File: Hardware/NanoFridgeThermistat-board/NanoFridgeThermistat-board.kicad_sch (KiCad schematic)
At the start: 18 parts, among them J1 Connector_Thermistor, J2 Main_Connector, J3 CompressorMotor_Connector, J4 I2C_Conn, U1 MOC3042M

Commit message: Improved routing for hardware
Signed-off-by: bebenlebricolo <benoittarrade@hotmail.fr>
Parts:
- D2: footprint (none) -> LED_THT:LED_D3.0mm
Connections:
- net Trigger: now reaches D1.3 (G), R3.2, U1.4
- net SnubberResLow: now reaches C1.1, R5.1, R6.1, R7.1, R8.1
- net NeutralTriac: now reaches C1.2, D1.1 (A1), J3.2 (Pin_2), R3.1
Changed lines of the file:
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@@
   (junction (at 186.69 60.96) (diameter 0) (color 0 0 0 0)
+  )
+  (junction (at 186.69 69.85) (diameter 0) (color 0 0 0 0)
   )
   (junction (at 186.69 57.15) (diameter 0) (color 0 0 0 0)
@@
     (stroke (width 0) (type default))
   )
+  (wire (pts (xy 181.61 69.85) (xy 186.69 69.85))
+    (stroke (width 0) (type default))
+  )
   (wire (pts (xy 151.13 57.15) (xy 162.56 57.15))
     (stroke (width 0) (type default))
@@
     (effects (font (size 1.27 1.27)) (justify left bottom))
   )
+  (label "Trigger" (at 146.05 62.23 0) (fields_autoplaced)
+    (effects (font (size 1 1)) (justify left bottom))
+  )
+  (label "SnubberResLow" (at 181.61 69.85 180) (fields_autoplaced)
+    (effects (font (size 1.27 1.27)) (justify right bottom))
+  )
+  (label "NeutralTriac" (at 162.56 74.93 0) (fields_autoplaced)
+    (effects (font (size 1 1)) (justify left bottom))
+  )
+  (label "LiveTriac" (at 154.94 57.15 0) (fields_autoplaced)
+    (effects (font (size 1 1)) (justify left bottom))
+  )
   (global_label "SDA" (shape input) (at 172.72 133.35 0) (fields_autoplaced)
     (effects (font (size 1.27 1.27)) (justify left))
@@
     (property "Intersheetrefs" "${INTERSHEET_REFS}" (at 186.9537 123.19 0)
       (effects (font (size 1.27 1.27)) (justify left) hide)
+    )
+  )
+  (netclass_flag "" (length 2.54) (shape round) (at 196.85 68.58 180)
+    (effects (font (size 1.27 1.27)) (justify right bottom))
+    (property "Netclass" "SnubberResLow" (at 195.58 72.39 0)
+      (effects (font (size 1 1) italic) (justify left))
     )
   )
@@
       (effects (font (size 1.27 1.27)))
     )
-    (property "Footprint" "" (at 119.38 76.2 0)
-      (effects (font (size 1.27 1.27)) hide)
-    )
+    (property "Footprint" "LED_THT:LED_D3.0mm" (at 119.38 76.2 0)
+      (effects (font (size 1.27 1.27)) hide)
+    )

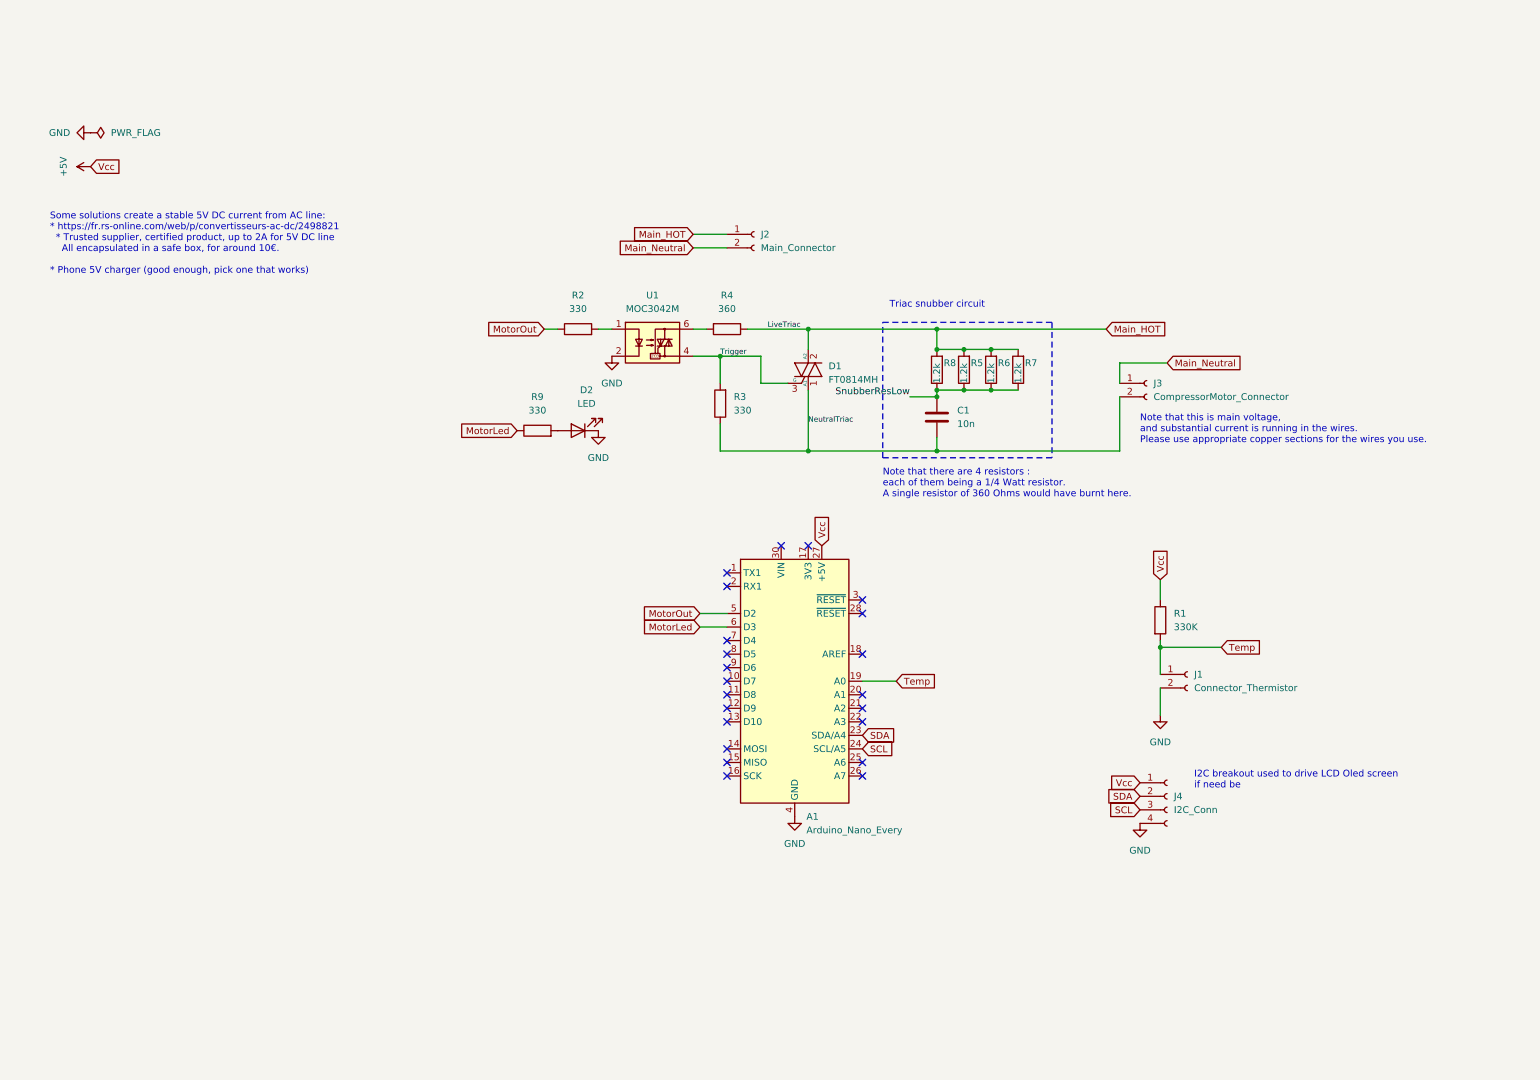
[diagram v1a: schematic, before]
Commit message: Added buttons and starting current sensor addition
Signed-off-by: bebenlebricolo <benoittarrade@hotmail.fr>
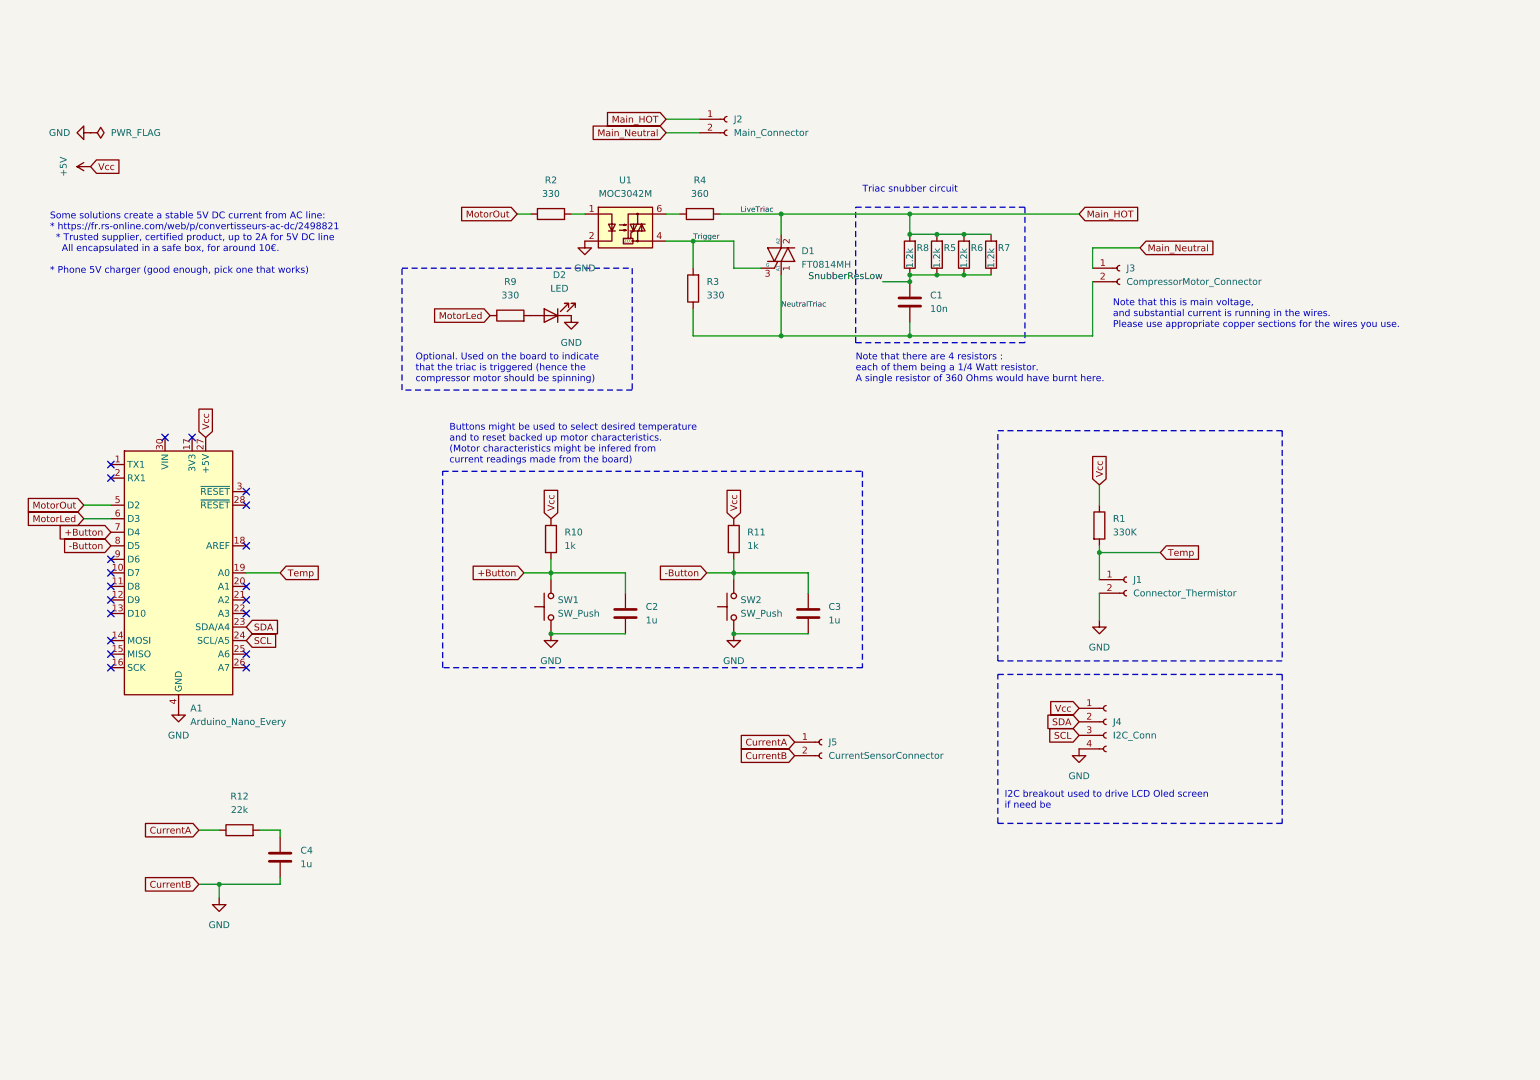
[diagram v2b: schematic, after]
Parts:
- added C2, C3, C4: 1u, symbol Device:C
- added J5: CurrentSensorConnector, Connector_PinSocket_2.54mm:PinSocket_1x02_P2.54mm_Vertical, symbol Connector:Conn_01x02_Socket
- added R10, R11: 1k, Resistor_THT:R_Axial_DIN0207_L6.3mm_D2.5mm_P10.16mm_Horizontal, symbol Device:R
- added R12: 22k, Resistor_THT:R_Axial_DIN0207_L6.3mm_D2.5mm_P10.16mm_Horizontal, symbol Device:R
- added SW1, SW2: SW_Push, symbol Switch:SW_Push
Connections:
- net +5V: now also R10.1, R11.1
- net GND: now also C2.2, C3.2, C4.2, J5.2 (Pin_2), SW1.1, SW2.1
- net +Button: now reaches A1.7 (D4)
- net +Button: now also C2.1, R10.2, SW1.2
- net -Button: now reaches A1.8 (D5)
- net -Button: now also C3.1, R11.2, SW2.2
- new net: C4.1, R12.2
- new net CurrentA: J5.1 (Pin_1), R12.1
- no-connect marks 22 -> 20
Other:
- note added: "Buttons might be used to select desired temperature and to reset backed up motor characteristics. (Motor characteristics might be infered from current readings made from the board)"
- note added: "Optional. Used on the board to indicate that the triac is triggered (hence the compressor motor should be spinning)"
- moved on the sheet: A1, C1, D1, D2, J1, J2, J3, J4, R1, R2, R3, R4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

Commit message: Added current sense hardware layout
Signed-off-by: bebenlebricolo <benoittarrade@hotmail.fr>
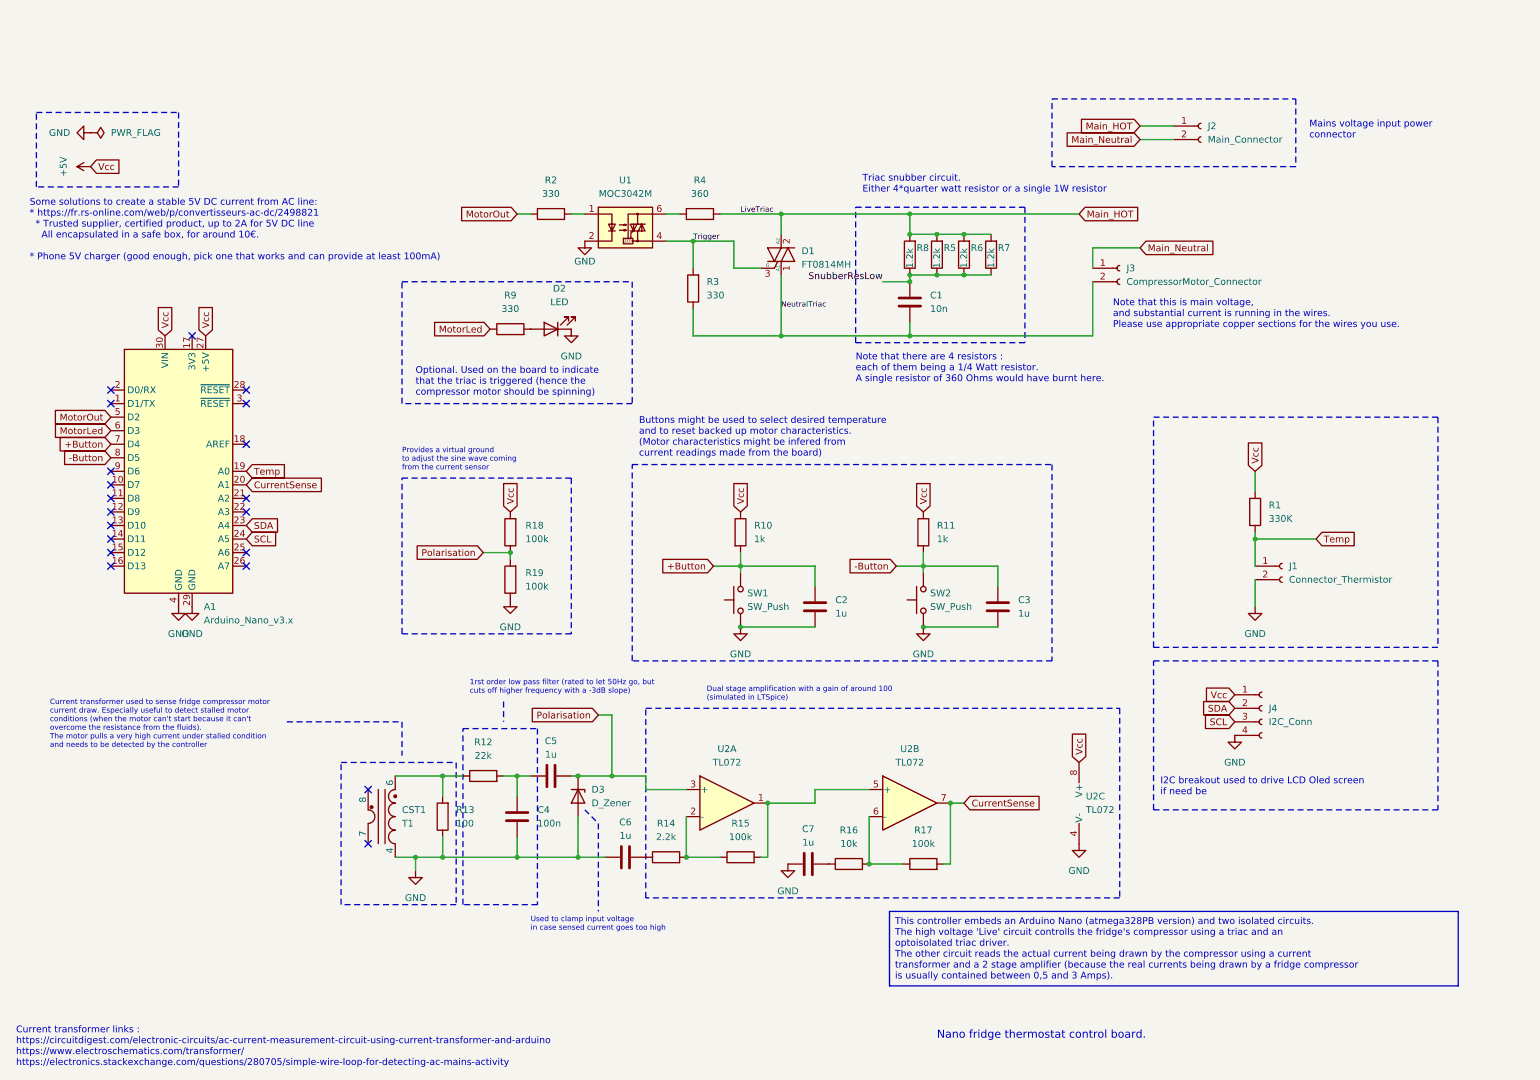
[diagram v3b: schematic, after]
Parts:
- removed A1: Arduino_Nano_Every, Module:Arduino_Nano, symbol MCU_Module:Arduino_Nano_Every
- removed J5: CurrentSensorConnector, Connector_PinSocket_2.54mm:PinSocket_1x02_P2.54mm_Vertical, symbol Connector:Conn_01x02_Socket
- added A1: Arduino_Nano_v3.x, Module:Arduino_Nano, symbol MCU_Module:Arduino_Nano_v3.x
- added C5, C6, C7: 1u, symbol Device:C
- added D3: D_Zener, symbol Device:D_Zener
- added R13: 100, Resistor_THT:R_Axial_DIN0207_L6.3mm_D2.5mm_P10.16mm_Horizontal, symbol Device:R
- added R14: 2.2k, Resistor_THT:R_Axial_DIN0207_L6.3mm_D2.5mm_P10.16mm_Horizontal, symbol Device:R
- added R15, R17, R18, R19: 100k, Resistor_THT:R_Axial_DIN0207_L6.3mm_D2.5mm_P10.16mm_Horizontal, symbol Device:R
- added R16: 10k, Resistor_THT:R_Axial_DIN0207_L6.3mm_D2.5mm_P10.16mm_Horizontal, symbol Device:R
- added T1: CST1, Transformer_SMD:Transformer_Coilcraft_CST1, symbol Transformer:CST1
- added U2: TL072, symbol Amplifier_Operational:TL072
- C4: value 1u -> 100n
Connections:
- net +5V: now also A1.27 (+5V), A1.30 (VIN), R18.2, U2.8 (V+)
- net +Button: now also A1.7 (D4)
- net -Button: now also A1.8 (D5)
- net GND: now also A1.29 (GND), A1.4 (GND), C6.1, C7.1, D3.2 (A), R13.1, R19.1, T1.4, U2.4 (V-)
- net MotorLed: now also A1.6 (D3)
- net MotorOut: now also A1.5 (D2)
- net SCL: now also A1.24 (A5)
- net SDA: now also A1.23 (A4)
- net Temp: now also A1.19 (A0)
- net at C4.1, R12.2: now also C5.1
- net CurrentA: no longer names the net of R12.1
- net CurrentA: now also R13.2, T1.6
- new net: C6.2, R14.1
- new net: R14.2, R15.1, U2.2 (-)
- new net: C7.2, R16.1
- new net: R15.2, U2.1, U2.5 (+)
- new net: R16.2, R17.1, U2.6 (-)
- new net CurrentSense: A1.20 (A1), R17.2, U2.7
- new net Polarisation: C5.2, D3.1 (K), R18.1, R19.2, U2.3 (+)
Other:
- note added: "1rst order low pass filter (rated to let 50Hz go, but cuts off higher frequency with a -3dB slope)"
- note added: "Current transformer links : https://circuitdigest.com/electronic-circuits/ac-current-measurement-circuit-using-current-transformer-and-arduino https://www.electroschematics.com/transformer/ https://electronics.stackexchange.com/questions/280705/simple-wire-loop-for-detecting-ac-mains-activity"
- note added: "Current transformer used to sense fridge compressor motor current draw. Especially useful to detect stalled motor conditions (when the motor can't start because it can't overcome the resistance from the fluids). The motor pulls a very high current under stalled condition and needs to be detected by the controller"
- note added: "Dual stage amplification with a gain of around 100 (simulated in LTSpice)"
- note added: "Mains voltage input power connector"
- note added: "Nano fridge thermostat control board."
- note added: "Provides a virtual ground to adjust the sine wave coming from the current sensor"
- note added: "Some solutions to create a stable 5V DC current from AC line: * https://fr.rs-online.com/web/p/convertisseurs-ac-dc/2498821 * Trusted supplier, certified product, up to 2A for 5V DC line All encapsulated in a safe box, for around 10€. * Phone 5V charger (good enough, pick one that works and can provide at least 100mA)"
- note added: "Triac snubber circuit. Either 4*quarter watt resistor or a single 1W resistor"
- note added: "Used to clamp input voltage in case sensed current goes too high"
- note removed: "Some solutions create a stable 5V DC current from AC line: * https://fr.rs-online.com/web/p/convertisseurs-ac-dc/2498821 * Trusted supplier, certified product, up to 2A for 5V DC line All encapsulated in a safe box, for around 10€. * Phone 5V charger (good enough, pick one that works)"
- note removed: "Triac snubber circuit"
- moved on the sheet: C2, C3, C4, D2, J1, J2, J4, R1, R10, R11, R12, R9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

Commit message: Added more parts sourcing
Signed-off-by: bebenlebricolo <benoittarrade@hotmail.fr>
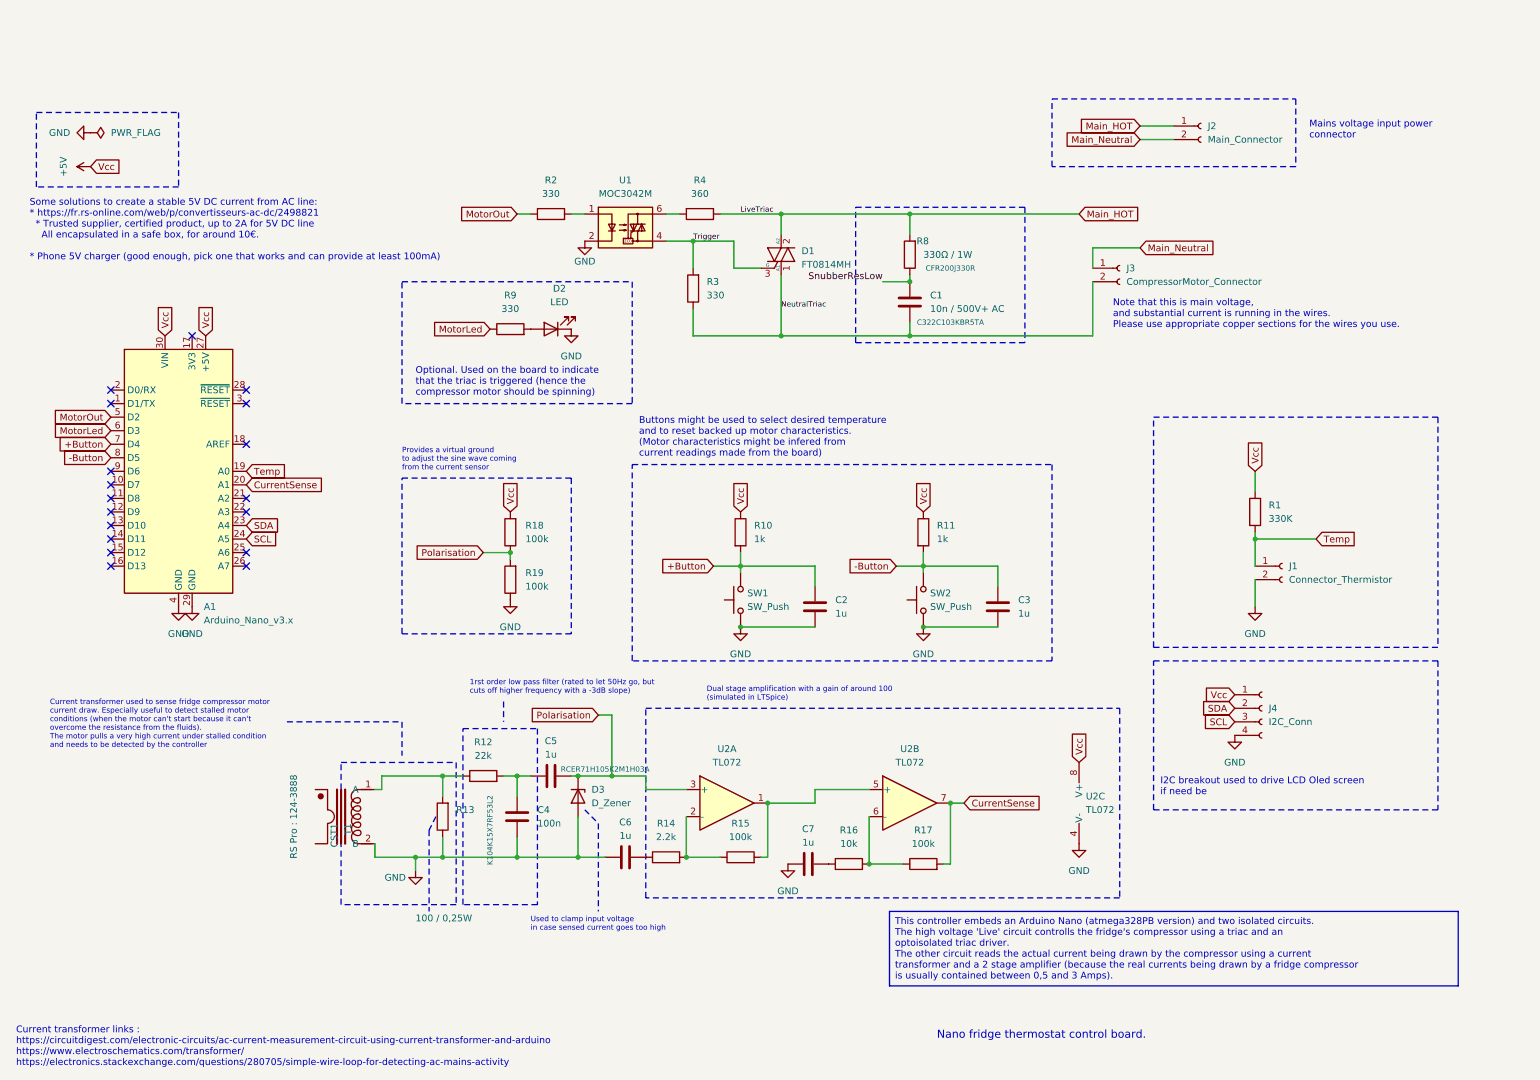
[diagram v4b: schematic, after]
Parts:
- removed R5, R6, R7: 1.2k, Resistor_THT:R_Axial_DIN0207_L6.3mm_D2.5mm_P10.16mm_Horizontal, symbol Device:R
- C1: value 10n -> 10n / 500V+ AC; footprint Capacitor_THT:C_Rect_L13.0mm_W4.0mm_P10.00mm_FKS3_FKP3_MKS4 -> Capacitor_THT:C_Disc_D10.0mm_W2.5mm_P5.00mm; Ref (none) -> C322C103KBR5TA
- C2, C3, C6, C7: footprint (none) -> Capacitor_THT:C_Disc_D4.7mm_W2.5mm_P5.00mm
- C4: footprint (none) -> Capacitor_THT:C_Disc_D3.8mm_W2.6mm_P2.50mm; Ref (none) -> K104K15X7RF53L2
- C5: footprint (none) -> Capacitor_THT:C_Disc_D4.7mm_W2.5mm_P5.00mm; Ref (none) -> RCER71H105K2M1H03A
- D3: footprint (none) -> Diode_THT:D_DO-35_SOD27_P7.62mm_Horizontal
- R13: value 100 -> 100 / 0,25W
- R8: value 1.2k -> 330Ω / 1W; footprint Resistor_THT:R_Axial_DIN0207_L6.3mm_D2.5mm_P10.16mm_Horizontal -> Resistor_THT:R_Axial_DIN0614_L14.3mm_D5.7mm_P20.32mm_Horizontal; Ref (none) -> CFR200J330R
- SW1, SW2: footprint (none) -> Button_Switch_THT:SW_PUSH_6mm
- T1: footprint Transformer_SMD:Transformer_Coilcraft_CST1 -> CurrentTransformer:CT-RSPRO-1243888; symbol Transformer:CST1 -> CurrentTransformers:CT-RSPRO-1243888; Ref (none) -> RS Pro : 124-3888
- U2: footprint (none) -> Package_DIP:DIP-8_W7.62mm
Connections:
- net GND: now also T1.2 (B); no longer T1.4
- net at R12.1, R13.2: now also T1.1 (A); no longer T1.6
- no-connect marks 20 -> 18
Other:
- note removed: "Note that there are 4 resistors : each of them being a 1/4 Watt resistor. A single resistor of 360 Ohms would have burnt here."
- note removed: "Triac snubber circuit. Either 4*quarter watt resistor or a single 1W resistor"
